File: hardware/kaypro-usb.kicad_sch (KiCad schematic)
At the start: 8 parts, among them J1 USB_A, J2 RJ11, U1 Pico

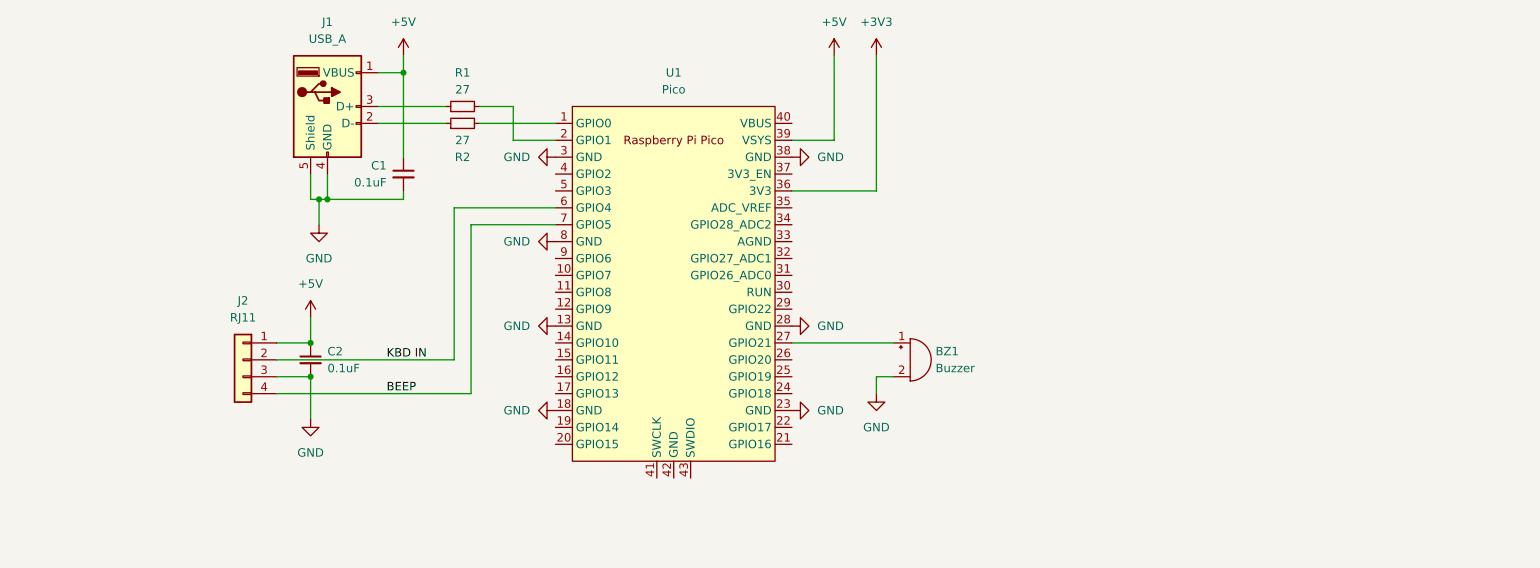
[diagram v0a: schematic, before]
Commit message: Added 6n137 optoisolator for level shifting. UART Tx inverted to complement 6n137 inversion.
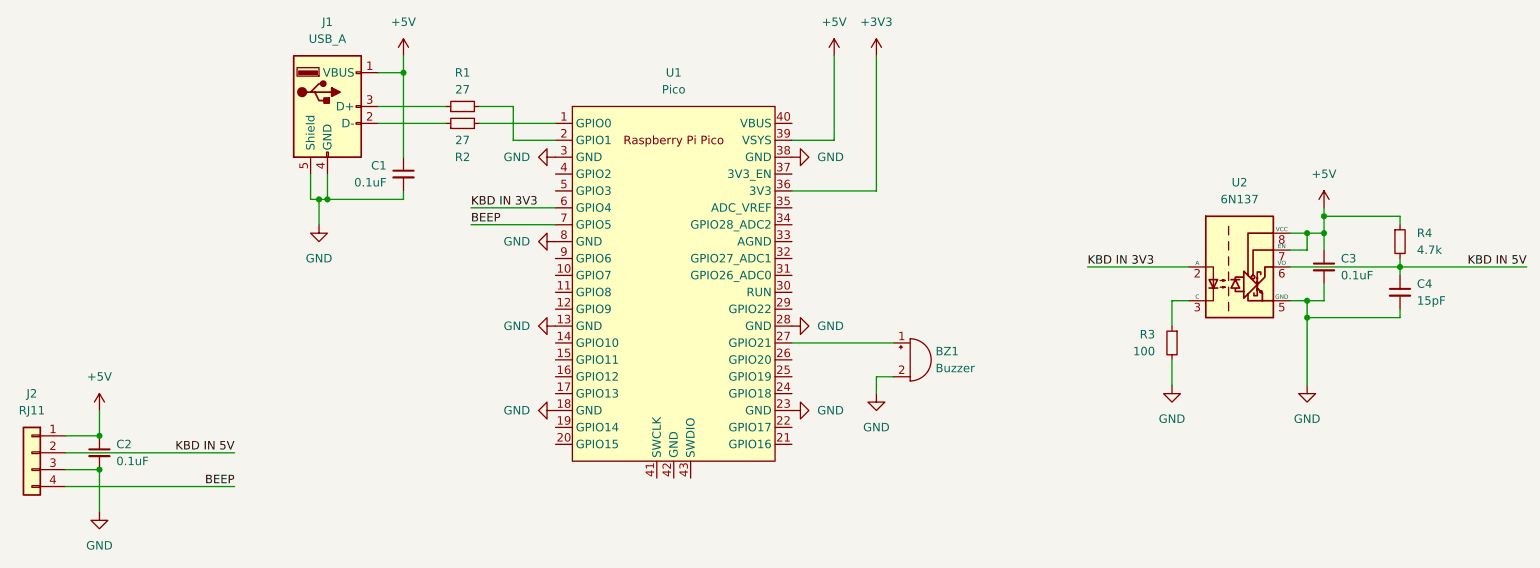
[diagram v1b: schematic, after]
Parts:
- added C3: 0.1uF, symbol Device:C_Small
- added C4: 15pF, symbol Device:C_Small
- added R3: 100, symbol Device:R_Small
- added R4: 4.7k, symbol Device:R_Small
- added U2: 6N137, Package_DIP:DIP-8_W7.62mm, symbol Isolator:6N137
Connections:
- net +5V: now also C3.1, R4.1, U2.7 (EN), U2.8 (VCC)
- net GND: now also C3.2, C4.2, R3.2, U2.5 (GND)
- net KBD IN renamed KBD IN 3V3
- net KBD IN 3V3: now also U2.2 (A); no longer J2.2 (Pin_2)
- new net: R3.1, U2.3 (C)
- new net KBD IN 5V: C4.1, J2.2 (Pin_2), R4.2, U2.6 (VO)
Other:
- company: (none) -> Cooper Dalrymple
- title: (none) -> kaypro-usb-keyboard-adapter
- moved on the sheet: C2, J2
